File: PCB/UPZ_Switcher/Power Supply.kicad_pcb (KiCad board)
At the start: 2 copper layers, 12 parts, among them IC1 TL783CKCSE3, U2 PR2301_TruePhantom, U3 PR2301_TruePhantom

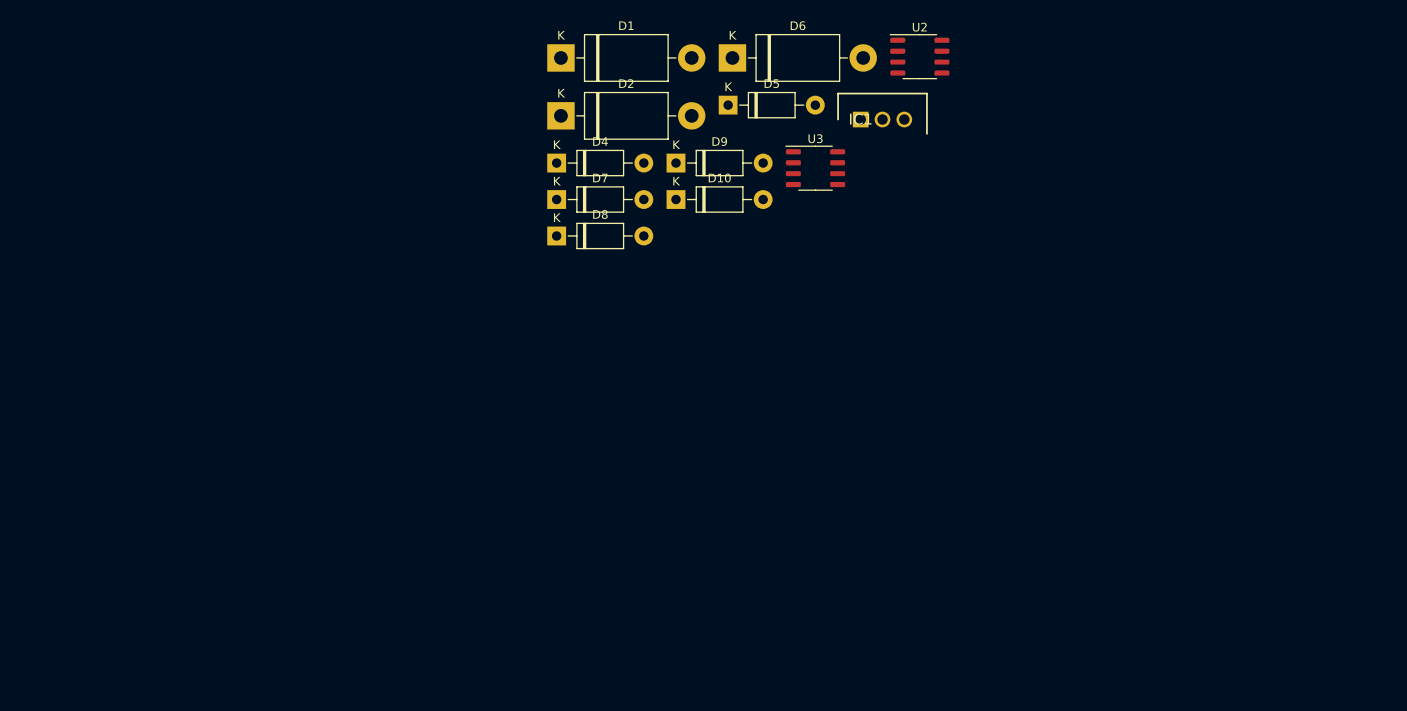
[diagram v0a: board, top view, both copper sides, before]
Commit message: update on power supply
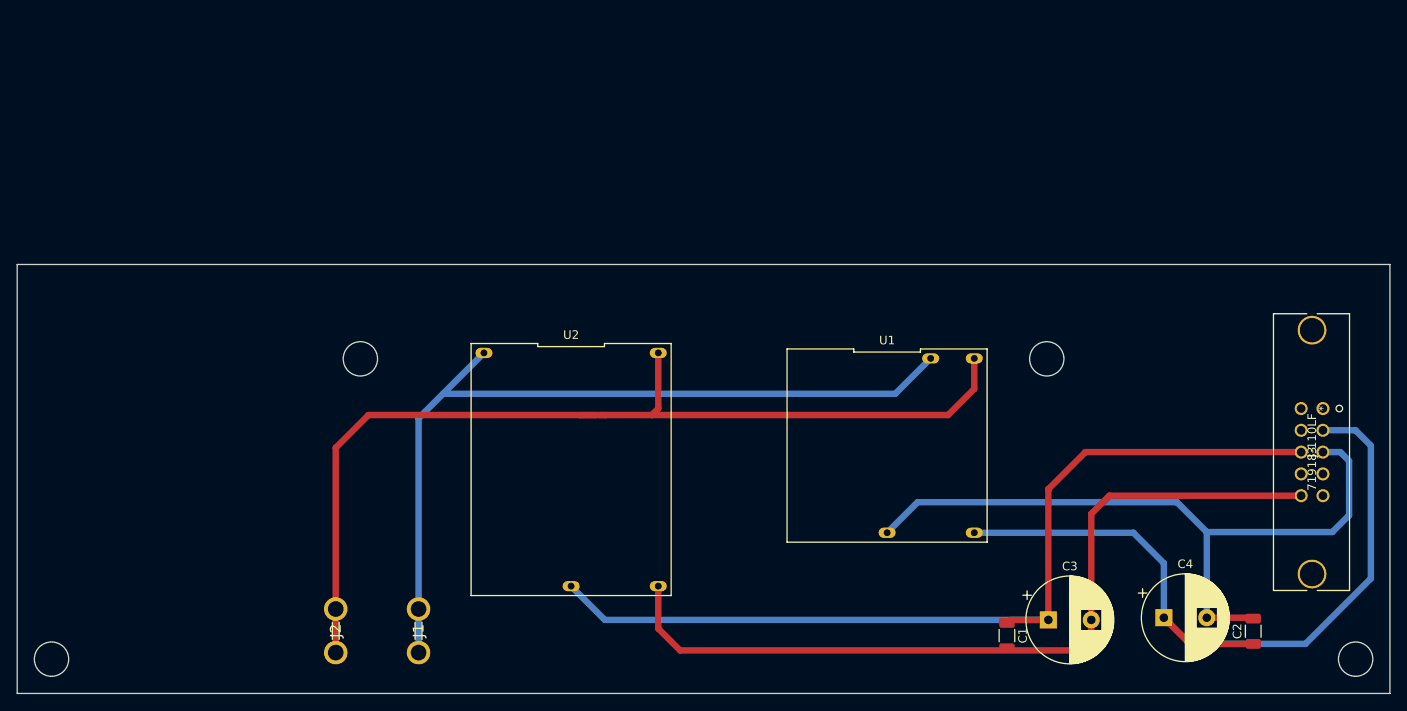
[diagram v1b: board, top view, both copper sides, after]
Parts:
- removed D1, D2, D6: 1N5408, Diode_THT:D_DO-201AD_P15.24mm_Horizontal
- removed D10, D4, D5, D7, D8, D9: 1N4007, Diode_THT:D_DO-41_SOD81_P10.16mm_Horizontal
- removed IC1: TL783CKCSE3, BVKSound:TO254P470X1016X1965-3P
- removed U3: PR2301_TruePhantom, Package_SO:SO-8_3.9x4.9mm_P1.27mm
- added C1: 100nF, Capacitor_SMD:C_1206_3216Metric, F.Cu at (188.2, 134.4)
- added C2: 100nF, Capacitor_SMD:C_1206_3216Metric, F.Cu at (216.9, 133.9)
- added C3: 100uF, Capacitor_THT:CP_Radial_D10.0mm_P5.00mm, F.Cu at (193.0, 132.6)
- added C4: 100uF, Capacitor_THT:CP_Radial_D10.0mm_P5.00mm, F.Cu at (206.5, 132.3)
- added J1: 1-726386-2, BVKSound:17263862, F.Cu at (119.6, 136.4)
- added J2: 1-726386-2, BVKSound:17263862, F.Cu at (110.0, 136.4)
- added J3: 71918-110LF, BVKSound:71918-110LF, F.Cu at (225.0, 108.0)
- added U1: MP-LD05-23B05R2, BVKSound:MP-LD05-23B05R2, F.Cu at (174.2, 112.3)
- U2: value PR2301_TruePhantom -> VCE05US48; footprint Package_SO:SO-8_3.9x4.9mm_P1.27mm -> BVKSound:VCE05US48
- moved U2 63.0 mm to (137.4, 115.1), turned to 270 degrees
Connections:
- U2 pad 1: GND1 -> Net-(J1-Pad1)
- U2 pad 2: GND1 -> Net-(J2-Pad1)
- U2 pad 3: Net-(C11-Pad2) -> Phantom_48V
- U2 pad 4: Net-(R3-Pad1) -> Phantom_48V_GND
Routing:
- net Net-(J2-Pad1): track 0.00 -> 114.9 mm
- net Phantom_48V: track 0.00 -> 108.7 mm
- net Phantom_48V_GND: track 0.00 -> 97.2 mm
- net Net-(J1-Pad1): track 0.00 -> 96.6 mm
- net 5V: track 0.00 -> 92.0 mm
- net 5V_GND: track 0.00 -> 82.8 mm
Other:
- board outline added: 160 x 50 mm

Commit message: final
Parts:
- J3: value 71918-110LF -> TO MCU BOARD
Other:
- board text added: "L"
- board text added: "N"
- board text added: "NET FILTER"
- board text added: "UPZ Switcher PSU Board BVKSound 2021-03"
